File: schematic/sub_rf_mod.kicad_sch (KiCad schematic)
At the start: 36 parts, among them J4B1 Conn_01x08

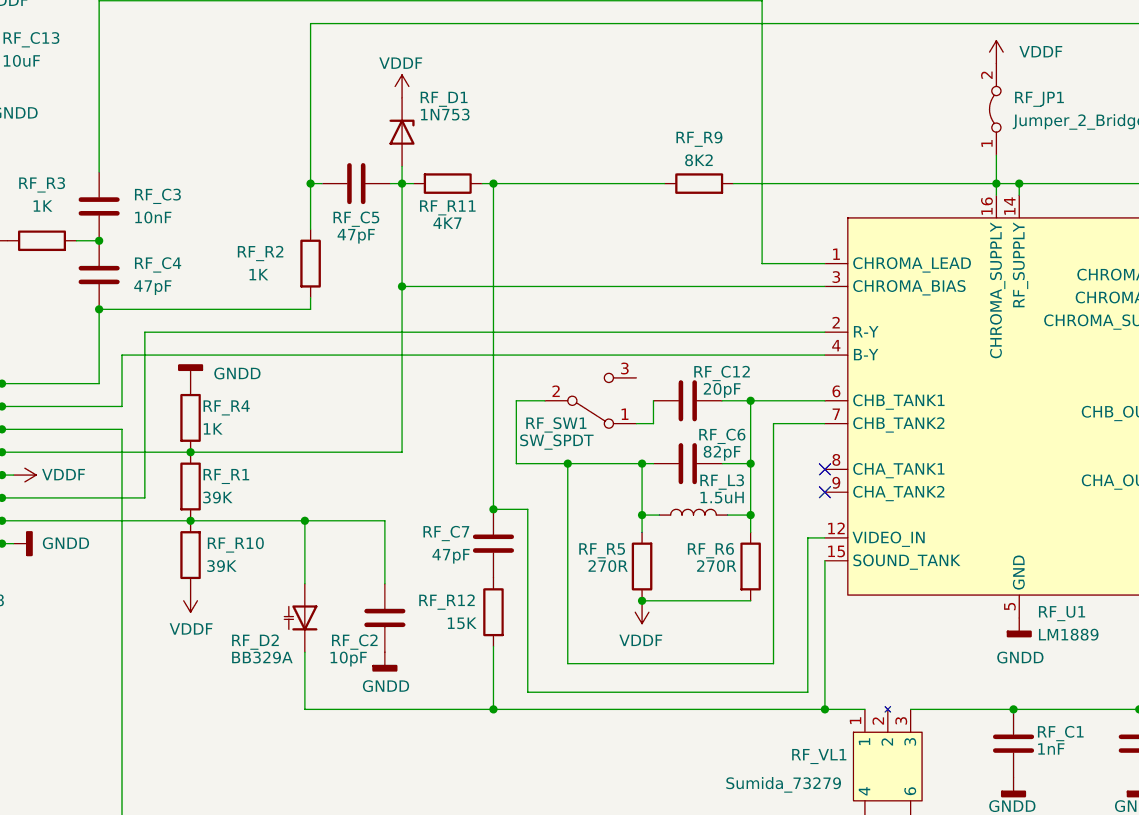
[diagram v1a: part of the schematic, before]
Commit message: added a new jack with matching pin names. started fixing drc errors. start working on power trace sizes.
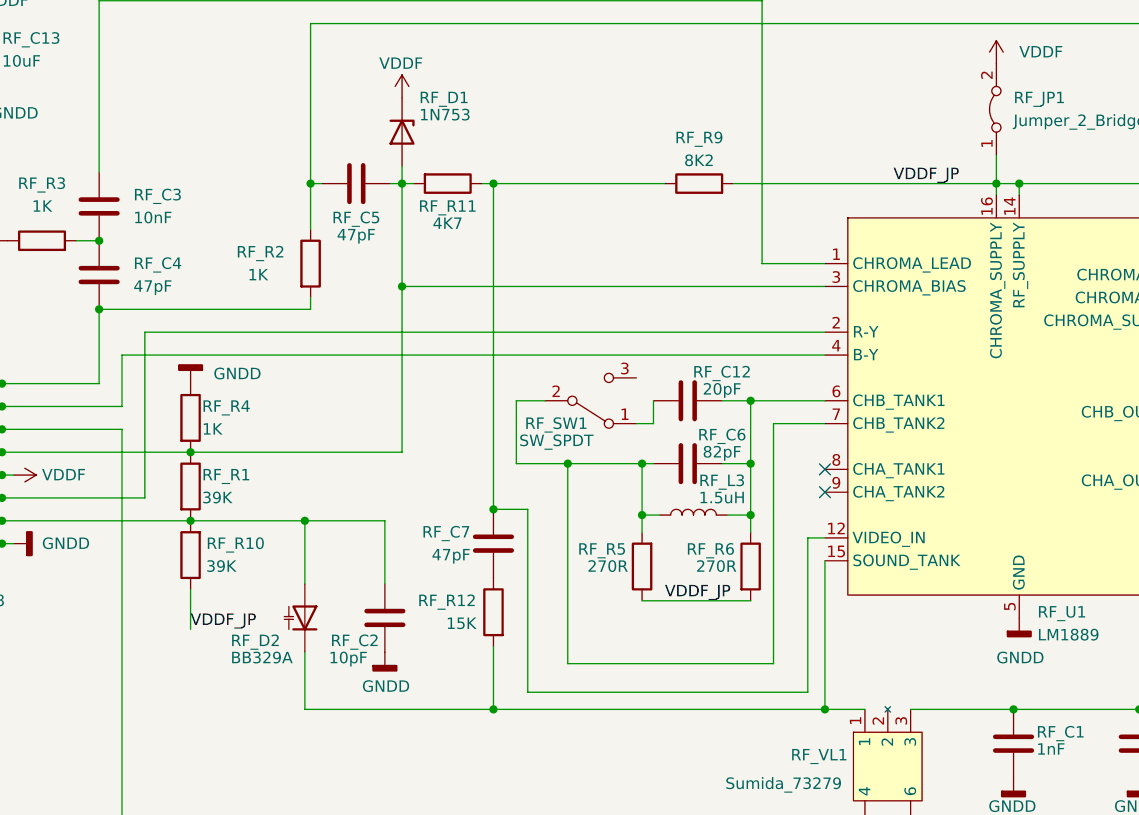
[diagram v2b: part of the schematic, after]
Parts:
- RF_J1: footprint RCJ-041:RCJ041 -> RCJ-041:RCJ041_copy
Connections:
- net VDDF: no longer RF_R10.1, RF_R5.1, RF_R6.2
- net VDDF_JP: now reaches RF_C1.1, RF_C8.1, RF_JP1.1 (A), RF_R8.2, RF_R9.2, RF_U1.14 (RF_SUPPLY), RF_U1.16 (CHROMA_SUPPLY), RF_VL1.3
- net VDDF_JP: now also RF_R10.1, RF_R5.1, RF_R6.2

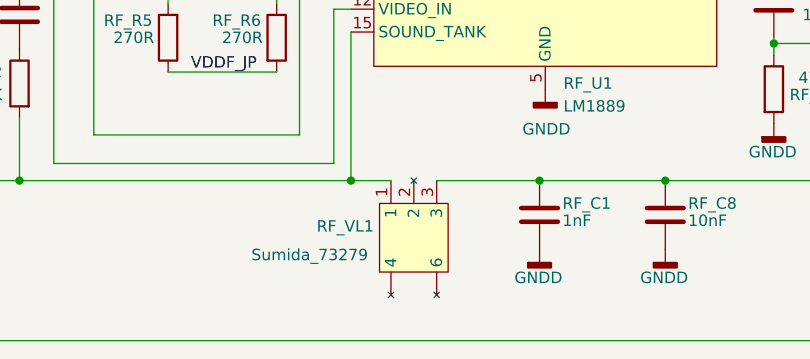
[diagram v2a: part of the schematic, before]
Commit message: added new models, fixed the drc errors. changed power width.
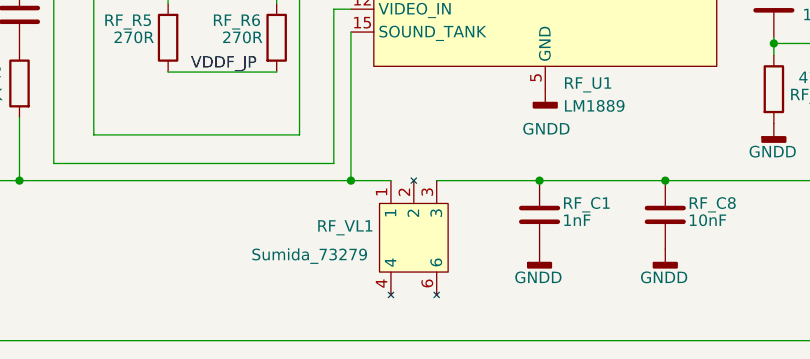
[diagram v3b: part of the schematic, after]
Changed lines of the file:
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@@
       (effects (font (size 1.27 1.27)) hide)
     )
-    (pin "")
-    (pin "")
     (pin "1")
     (pin "2")
     (pin "3")
+    (pin "4")
     (pin "5")
+    (pin "6")
   )
   (symbol (lib_id "Device:C_Polarized") (at 39.37 53.975 0) (unit 1)

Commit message: updated schematic with new layout
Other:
- company: (none) -> sparkletron
- title: Colecovision Schematic -> Reverse Engineer Colecovision
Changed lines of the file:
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@@
   (paper "USLetter")
   (title_block
-    (title "Colecovision Schematic")
-    (date "2023-01-09")
-    (rev "E.0")
+    (title "Reverse Engineer Colecovision")
+    (date "2023-03-14")
+    (rev "DEV")
+    (company "sparkletron")
     (comment 1 "Jay Convertino")
+    (comment 2 "MIT LICENSE")
   )
   (junction (at 43.18 100.33) (diameter 0) (color 0 0 0 0)

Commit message: change connector to female
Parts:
- J4B1: footprint Connector_PinHeader_2.54mm:PinHeader_1x08_P2.54mm_Vertical -> Connector_PinSocket_2.54mm:PinSocket_1x08_P2.54mm_Vertical
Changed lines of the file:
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@@
     (property "Reference" "J4B1" (id 0) (at 38.1 111.76 0))
     (property "Value" "Conn_01x08" (id 1) (at 38.1 114.3 0))
-    (property "Footprint" "Connector_PinHeader_2.54mm:PinHeader_1x08_P2.54mm_Vertical" (id 2) (at 38.1 100.33 0)
+    (property "Footprint" "Connector_PinSocket_2.54mm:PinSocket_1x08_P2.54mm_Vertical" (id 2) (at 38.1 100.33 0)
       (effects (font (size 1.27 1.27)) hide)
     )

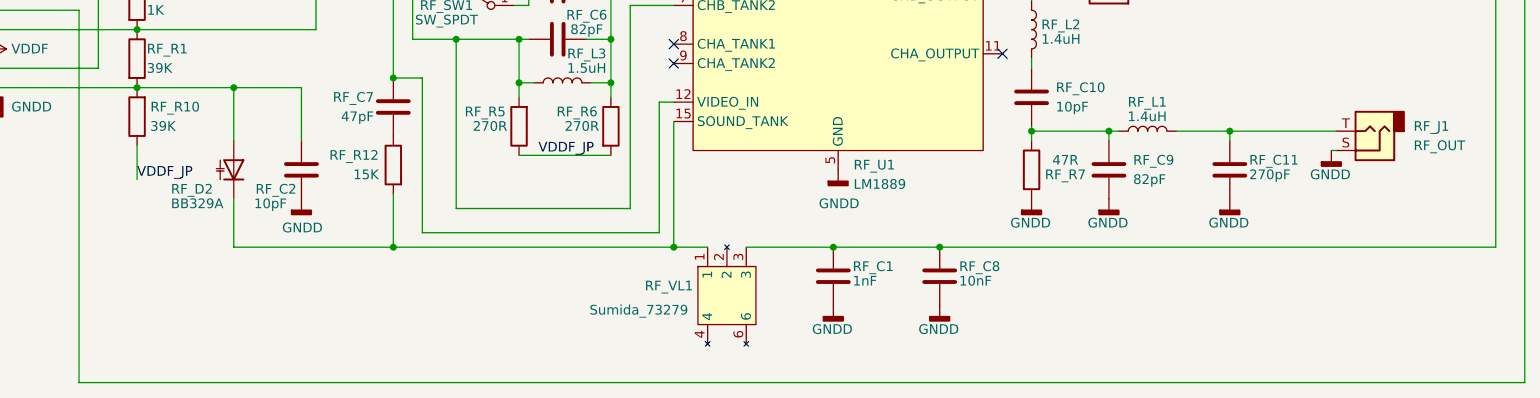
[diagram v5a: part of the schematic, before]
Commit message: added pads for switch and RF shield, RF shield still needs adjustment
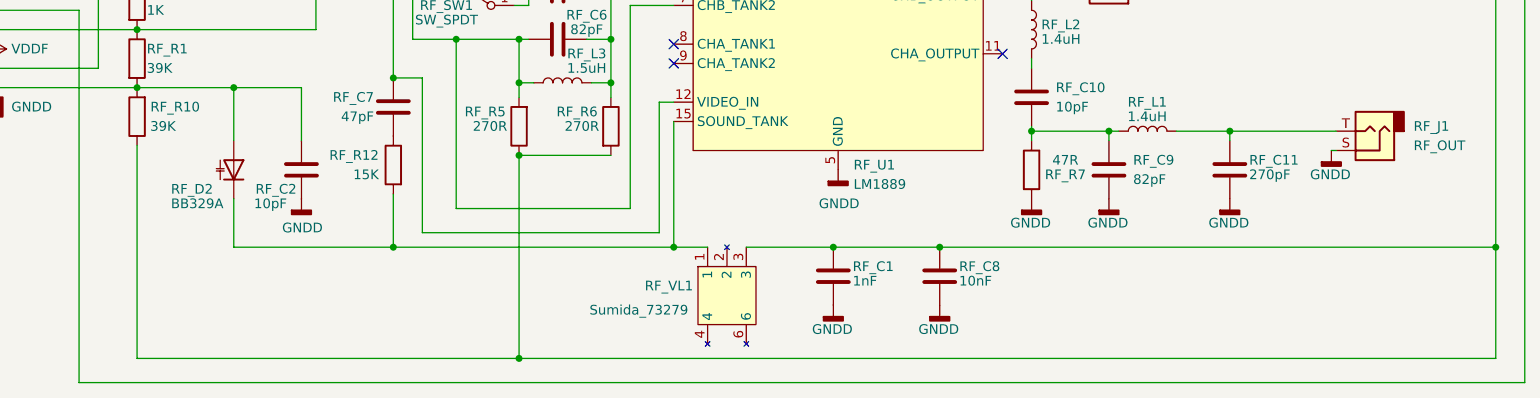
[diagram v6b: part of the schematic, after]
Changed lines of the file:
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@@
     (comment 2 "MIT LICENSE")
   )
+  (junction (at 242.57 126.365) (diameter 0) (color 0 0 0 0)
+  )
   (junction (at 43.18 100.33) (diameter 0) (color 0 0 0 0)
   )
@@
   (junction (at 153.67 67.945) (diameter 0) (color 0 0 0 0)
   )
+  (junction (at 114.3 140.97) (diameter 0) (color 0 0 0 0)
+  )
   (junction (at 64.135 97.79) (diameter 0) (color 0 0 0 0)
   )
@@
   )
   (junction (at 43.18 105.41) (diameter 0) (color 0 0 0 0)
+  )
+  (junction (at 114.3 114.3) (diameter 0) (color 0 0 0 0)
   )
   (junction (at 43.18 95.25) (diameter 0) (color 0 0 0 0)
@@
     (stroke (width 0) (type default) (color 0 0 0 0))
   )
-  (wire (pts (xy 64.135 113.03) (xy 64.135 117.475))
-    (stroke (width 0) (type default) (color 0 0 0 0))
-  )
   (wire (pts (xy 44.45 107.95) (xy 43.18 107.95))
     (stroke (width 0) (type default) (color 0 0 0 0))
@@
     (stroke (width 0) (type default) (color 0 0 0 0))
   )
+  (wire (pts (xy 97.79 126.365) (xy 134.62 126.365))
+    (stroke (width 0) (type default) (color 0 0 0 0))
+  )
   (wire (pts (xy 43.18 97.79) (xy 64.135 97.79))
     (stroke (width 0) (type default) (color 0 0 0 0))
@@
     (stroke (width 0) (type default) (color 0 0 0 0))
   )
+  (wire (pts (xy 114.3 140.97) (xy 64.135 140.97))
+    (stroke (width 0) (type default) (color 0 0 0 0))
+  )
   (wire (pts (xy 86.36 67.945) (xy 87.63 67.945))
     (stroke (width 0) (type default) (color 0 0 0 0))
@@
     (stroke (width 0) (type default) (color 0 0 0 0))
   )
+  (wire (pts (xy 64.135 113.03) (xy 64.135 140.97))
+    (stroke (width 0) (type default) (color 0 0 0 0))
+  )
   (wire (pts (xy 51.435 74.295) (xy 53.975 74.295))
     (stroke (width 0) (type default) (color 0 0 0 0))
@@
     (stroke (width 0) (type default) (color 0 0 0 0))
   )
+  (wire (pts (xy 242.57 126.365) (xy 242.57 140.97))
+    (stroke (width 0) (type default) (color 0 0 0 0))
+  )
   (wire (pts (xy 195.58 93.345) (xy 242.57 93.345))
     (stroke (width 0) (type default) (color 0 0 0 0))
@@
     (stroke (width 0) (type default) (color 0 0 0 0))
   )
-  (wire (pts (xy 97.79 126.365) (xy 134.62 126.365))
-    (stroke (width 0) (type default) (color 0 0 0 0))
-  )
   (wire (pts (xy 124.46 67.945) (xy 153.67 67.945))
     (stroke (width 0) (type default) (color 0 0 0 0))
@@
     (stroke (width 0) (type default) (color 0 0 0 0))
   )
+  (wire (pts (xy 242.57 140.97) (xy 114.3 140.97))
+    (stroke (width 0) (type default) (color 0 0 0 0))
+  )
   (wire (pts (xy 246.38 144.145) (xy 246.38 83.185))
     (stroke (width 0) (type default) (color 0 0 0 0))
@@
     (stroke (width 0) (type default) (color 0 0 0 0))
   )
-  (label "VDDF_JP" (at 64.135 117.475 0)
-    (effects (font (size 1.27 1.27)) (justify left bottom))
-  )
-  (label "VDDF_JP" (at 116.84 114.3 0)
-    (effects (font (size 1.27 1.27)) (justify left bottom))
+  (wire (pts (xy 114.3 114.3) (xy 114.3 140.97))
+    (stroke (width 0) (type default) (color 0 0 0 0))
   )
   (label "VDDF_JP" (at 142.24 67.945 0)

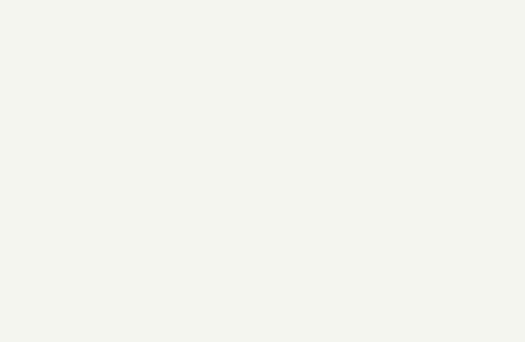
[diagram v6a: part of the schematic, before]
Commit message: fixed mount spacing, added labels, and added new version of reset switch.
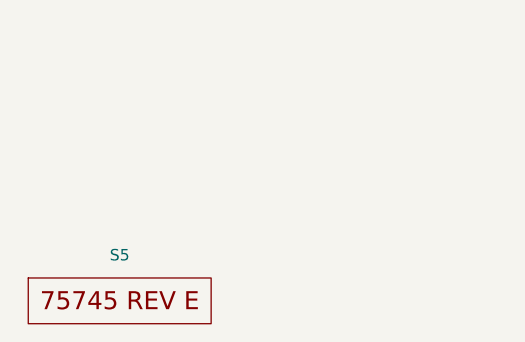
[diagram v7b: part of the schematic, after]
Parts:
- added S5: rf_board_rev, logos:rf_board_revision, symbol logos:rf_board_rev
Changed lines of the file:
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@@
     (pin "2")
+  )
+  (symbol (lib_id "logos:rf_board_rev") (at 24.13 196.85 0) (unit 1)
+    (in_bom yes) (on_board yes) (fields_autoplaced)
+    (property "Reference" "S5" (id 0) (at 25.4 193.04 0))
+    (property "Value" "rf_board_rev" (id 1) (at 24.13 191.77 0)
+      (effects (font (size 1.27 1.27)) hide)
+    )
+    (property "Footprint" "logos:rf_board_revision" (id 2) (at 24.13 196.85 0)
+      (effects (font (size 1.27 1.27)) hide)
+    )
+    (property "Datasheet" "" (id 3) (at 24.13 196.85 0)
+      (effects (font (size 1.27 1.27)) hide)
+    )
   )
   (symbol (lib_id "Device:R") (at 191.77 93.345 90) (unit 1)

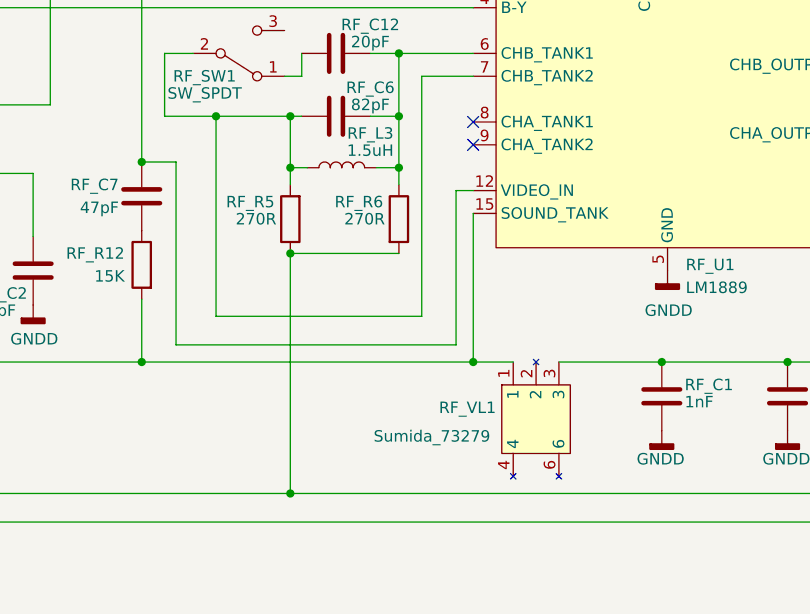
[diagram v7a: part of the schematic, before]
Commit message: imporved power rails, added 3D models (primitives at this point till others can be made).
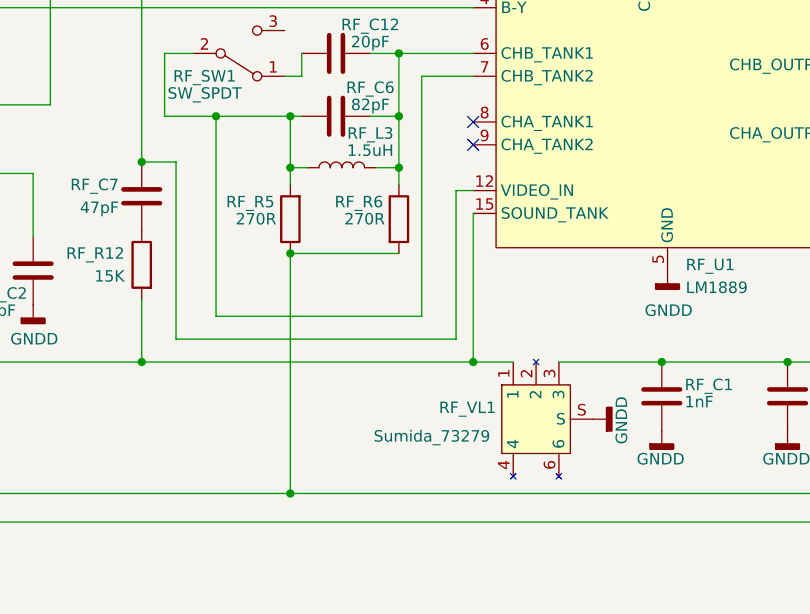
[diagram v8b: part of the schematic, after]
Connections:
- net GNDD: now also RF_VL1.S
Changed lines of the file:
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@@
     (stroke (width 0) (type default) (color 0 0 0 0))
   )
-  (wire (pts (xy 132.715 107.315) (xy 132.715 124.46))
+  (wire (pts (xy 132.715 107.315) (xy 132.715 123.825))
     (stroke (width 0) (type default) (color 0 0 0 0))
   )
@@
     (stroke (width 0) (type default) (color 0 0 0 0))
   )
-  (wire (pts (xy 101.6 104.14) (xy 101.6 124.46))
+  (wire (pts (xy 101.6 104.14) (xy 101.6 123.825))
     (stroke (width 0) (type default) (color 0 0 0 0))
   )
@@
     (stroke (width 0) (type default) (color 0 0 0 0))
   )
-  (wire (pts (xy 101.6 124.46) (xy 132.715 124.46))
+  (wire (pts (xy 101.6 123.825) (xy 132.715 123.825))
     (stroke (width 0) (type default) (color 0 0 0 0))
   )
@@
     (pin "1")
     (pin "2")
+  )
+  (symbol (lib_id "power:GNDD") (at 147.955 132.715 90) (unit 1)
+    (in_bom yes) (on_board yes)
+    (property "Reference" "#PWR?" (id 0) (at 154.305 132.715 0)
+      (effects (font (size 1.27 1.27)) hide)
+    )
+    (property "Value" "GNDD" (id 1) (at 151.13 130.175 0)
+      (effects (font (size 1.27 1.27)) (justify right))
+    )
+    (property "Footprint" "" (id 2) (at 147.955 132.715 0)
+      (effects (font (size 1.27 1.27)) hide)
+    )
+    (property "Datasheet" "" (id 3) (at 147.955 132.715 0)
+      (effects (font (size 1.27 1.27)) hide)
+    )
+    (pin "1")
   )
   (symbol (lib_id "Device:D_Zener") (at 87.63 62.23 270) (unit 1)
@@
     (pin "5")
     (pin "6")
+    (pin "S")
   )
   (symbol (lib_id "Device:C_Polarized") (at 39.37 53.975 0) (unit 1)
